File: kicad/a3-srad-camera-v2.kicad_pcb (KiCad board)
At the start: 4 copper layers, 50 x 50 mm, 179 parts, among them J1 Amphenol F32Q 1x22 P=0.5mm, J2 BOARD_IND, J3 OUT, SW1 PWRON, U1 AMS1117-3.3, U2 TPS6521905RHBR, U3 STM32U073R8Tx, U4 RV1106G2

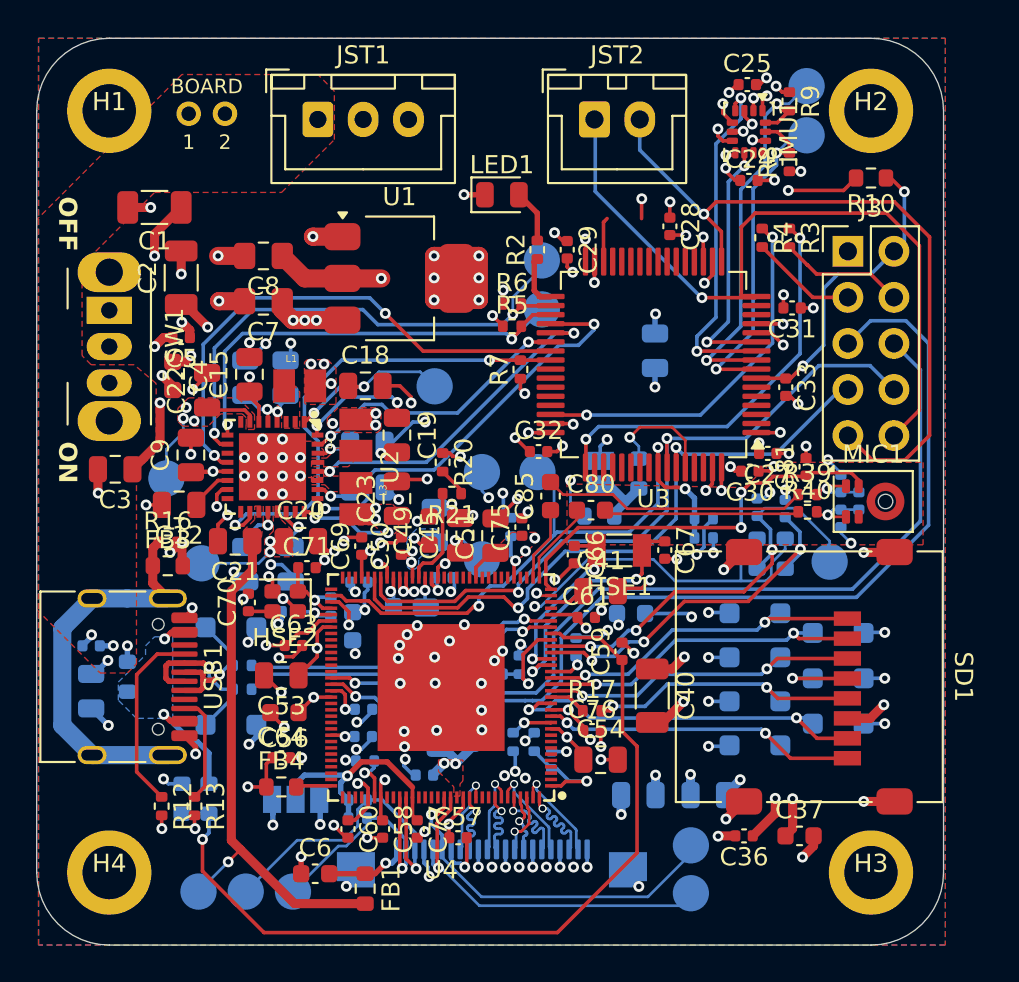
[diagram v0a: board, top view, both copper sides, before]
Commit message: Footprint + silkscreen corrections
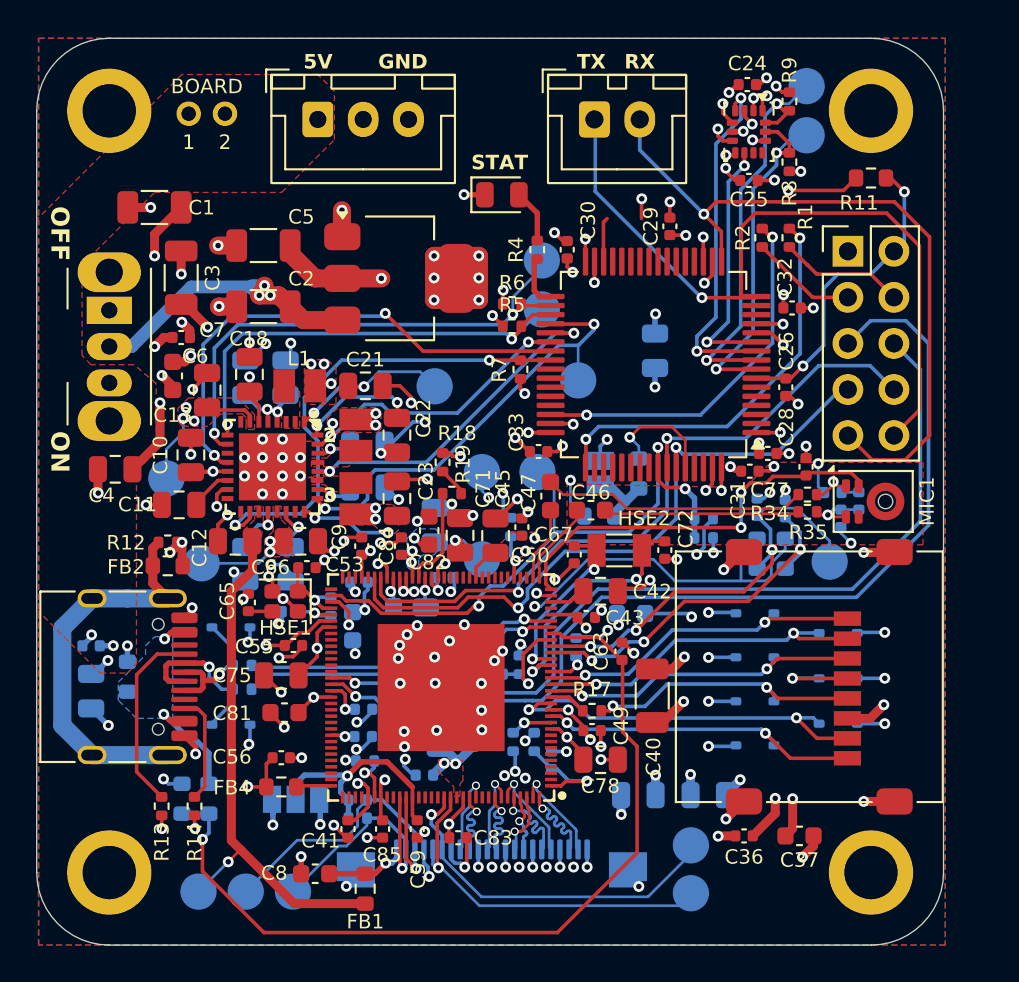
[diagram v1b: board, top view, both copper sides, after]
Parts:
- added TP9: TestPoint, a3-srad-camera-v2:TestPoint_Pad_D2.0mm_Small_Courtyard, B.Cu at (156.9, 94.9)
- C2: renamed from C7; footprint Capacitor_SMD:C_0805_2012Metric_Pad1.18x1.45mm_HandSolder -> Capacitor_SMD:C_1206_3216Metric
- C5: renamed from C8; footprint Capacitor_SMD:C_0805_2012Metric_Pad1.18x1.45mm_HandSolder -> Capacitor_SMD:C_1206_3216Metric
- D1, D2, D3, D4, D5, D6, D7, D8, D9: footprint Diode_SMD:D_SOD-123F -> Diode_SMD:D_SOD-323
- R4: renamed from R2; value ? -> 120R
- moved C68 0.67 mm to (170.9, 101.0), turned to 0 degrees
- moved C5 0.57 mm to (139.5, 87.4)
- moved C2 0.30 mm to (139.5, 90.8)
- renumbered C9 to C10, C12 to C11, C21 to C12, C22 to C13, C10 to C14, C11 to C15, C13 to C16, C14 to C17, C15 to C18, C16 to C19, C17 to C20, C18 to C21, C19 to C22, C25 to C24, C24 to C25, C33 to C26, C26 to C27, C27 to C28, C28 to C29, C2 to C3, C29 to C30, C30 to C31, C31 to C32, C32 to C33, C3 to C4, C60 to C41, C41 to C42, C61 to C43, C62 to C44, C51 to C45, C80 to C46, C85 to C47, C72 to C48, C76 to C49, C75 to C50, C73 to C51, C68 to C52, C69 to C53, C74 to C54, C63 to C55, C64 to C56, C65 to C57, C79 to C58, C77 to C59, C4 to C6, C78 to C60, C42 to C61, C43 to C62, C59 to C63, C44 to C64, C70 to C65, C71 to C66, C66 to C67, C83 to C68, C82 to C69, C5 to C7, C84 to C70, C45 to C71, C67 to C72, C52 to C73, C46 to C74, C53 to C75, C47 to C76, C81 to C77, C54 to C78, C55 to C79, C6 to C8, C48 to C80, C56 to C81, C49 to C82, C57 to C83, C50 to C84, C58 to C85, C20 to C9, FB3 to FB2, FB2 to FB3, H3 to H2, H2 to H3, HSE2 to HSE1, HSE1 to HSE2, J3 to J1, J1 to J2, J2 to J3, R3 to R1, R11 to R10, R10 to R11, R16 to R12, R12 to R13, R13 to R14, R14 to R15, R15 to R16, R20 to R18, R21 to R19, R4 to R2, R24 to R20, R18 to R21, R23 to R22, R27 to R23, R34 to R24, R30 to R25, R31 to R26, R32 to R27, R33 to R28, R37 to R29, R1 to R3, R35 to R30, R36 to R31, R19 to R32, R22 to R33, R39 to R34, R40 to R35, R28 to R36, R25 to R37, R29 to R38, R26 to R39, TP2 to TP10, TP4 to TP11, TP7 to TP12, TP9 to TP13, TP11 to TP14, TP12 to TP15, TP14 to TP16, TP16 to TP17, TP3 to TP2, TP5 to TP3, TP6 to TP4, TP8 to TP5, TP10 to TP6, TP13 to TP7, TP15 to TP8
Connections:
- C1 pad 1: VSYS_5V0 -> VIN_5V
- C10 pad 1: VSYS_5V0 -> VIN_5V
- C14 pad 1: VSYS_5V0 -> VIN_5V
- C15 pad 1: VSYS_5V0 -> VIN_5V
- C16 pad 1: VSYS_5V0 -> VIN_5V
- C17 pad 1: VSYS_5V0 -> VIN_5V
- C18 pad 1: VSYS_5V0 -> VIN_5V
- C19 pad 1: VSYS_5V0 -> VIN_5V
- C20 pad 1: VSYS_5V0 -> VIN_5V
- C3 pad 1: VSYS_5V0 -> VIN_5V
- C34 pad 2: /VIN_5V -> VIN_5V
- C35 pad 2: /VIN_5V -> VIN_5V
- C4 pad 1: VSYS_5V0 -> VIN_5V
- C6 pad 1: VSYS_5V0 -> VIN_5V
- C7 pad 2: VSYS_5V0 -> VIN_5V
- FB3 pad 1: /VIN_5V -> VIN_5V
- JST1 pad 1: /VIN_5V -> VIN_5V
- SW1 pad 3: /VIN_5V -> VIN_5V
- U2 pad 13: VSYS_5V0 -> VIN_5V
- U2 pad 20: VSYS_5V0 -> VIN_5V
- U2 pad 22: VSYS_5V0 -> VIN_5V
- U2 pad 26: VSYS_5V0 -> VIN_5V
- U2 pad 30: VSYS_5V0 -> VIN_5V
- U2 pad 4: VSYS_5V0 -> VIN_5V
- U2 pad 5: VSYS_5V0 -> VIN_5V
- U2 pad 6: VSYS_5V0 -> VIN_5V
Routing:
- net VIN_5V: track 0.00 -> 34.2 mm, vias 0 -> 16
- net VSYS_5V0: track 35.4 -> 17.7 mm, vias 16 -> 3
- net /VIN_5V: track 2.86 -> 0.00 mm, vias 3 -> 0
- net GND: track 154.3 -> 156.5 mm
- net /EN: track 23.1 -> 25.0 mm
- net /VSEL: track 28.7 -> 28.0 mm
- net /SCL: track 29.8 -> 29.1 mm
- added copper zone on F.Cu, net VIN_5V
- added copper zone on In1.Cu, net VIN_5V
- removed copper zone on F.Cu, net /VIN_5V
- removed copper zone on In1.Cu, net VSYS_5V0
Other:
- board text added: "2"
- board text added: "3"
- board text added: "5V"
- board text added: "CLK"
- board text added: "DIO"
- board text added: "FC"
- board text added: "GND"
- board text added: "RST"
- board text added: "RV"
- board text added: "RX"
- board text added: "STAT"
- board text added: "STM"
- board text added: "TX"

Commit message: Final changes before order
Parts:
- removed C68, C69, C70: 100pF, Capacitor_SMD:C_0402_1005Metric
- removed C77: 100nF, Capacitor_SMD:C_0402_1005Metric
- removed R34, R35: 22k, Resistor_SMD:R_0402_1005Metric
- added C86: 100nF, Capacitor_SMD:C_0402_1005Metric, B.Cu at (170.3, 101.1)
- added C87: 15pF, Capacitor_SMD:C_0402_1005Metric, B.Cu at (170.3, 102.0)
- added FB5: 120R, Resistor_SMD:R_0603_1608Metric, F.Cu at (169.8, 100.4)
- added R40: DNP, Resistor_SMD:R_0402_1005Metric, B.Cu at (159.4, 89.0)
- added R41: DNP, Resistor_SMD:R_0402_1005Metric, B.Cu at (159.4, 90.3)
- added R42: 10k, Resistor_SMD:R_0402_1005Metric, F.Cu at (151.4, 95.9)
- added R43: DNP, Resistor_SMD:R_0402_1005Metric, F.Cu at (151.4, 94.9)
- C46, C47: value 1uF -> 100nF; footprint Capacitor_SMD:C_0603_1608Metric -> Capacitor_SMD:C_0402_1005Metric
- MIC1: value IM73A135V01 -> CMM-2718AB-3815NC-TR; footprint Sensor_Audio:Infineon_PG-LLGA-5-2 -> a3-srad-camera-v2:MIC_CMM-2718AB-3815NC-TR
- moved C47 0.38 mm to (155.3, 101.6)
- moved C46 0.18 mm to (157.6, 102.2)
- moved MIC1 0.12 mm to (173.0, 101.5), turned to 90 degrees
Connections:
- net /STM32U575RGT6/BOOT0 renamed /STM32U073x/BOOT0
- net /STM32U575RGT6/LED renamed /STM32U073x/LED
- net /STM32U575RGT6/SWCLK renamed /STM32U073x/SWCLK
- net /STM32U575RGT6/SWDIO renamed /STM32U073x/SWDIO
- net /TPS6521905RHBR/LX_B1_1 renamed /TPS65219x/LX_B1
- net /TPS6521905RHBR/LX_B2 renamed /TPS65219x/LX_B2
- net /TPS6521905RHBR/LX_B3 renamed /TPS65219x/LX_B3
- MIC1 pad 2: /RV1106G2 SoC/VCC1V8_MICBIAS -> /RV1106G2 SoC/CODEC_MIC0P
- MIC1 pad 3: Net-(MIC1-OUT-) -> GND
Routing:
- net /RV1106G2 SoC/CODEC_MIC0N: track 10.8 -> 15.4 mm
- net /RV1106G2 SoC/VCC1V8_MICBIAS: track 22.6 -> 18.6 mm
- net Net-(MIC1-OUT-): track 3.56 -> 0.00 mm, vias 1 -> 0
- net VSYS_3V3: track 43.7 -> 47.2 mm, vias 32 -> 34
- net /EN: track 25.0 -> 28.3 mm
- net /VDD_CPU: track 12.1 -> 8.80 mm
- net /RV1106G2 SoC/CODEC_MIC0P: track 14.6 -> 17.7 mm, vias 0 -> 1
- net /VSEL: track 28.0 -> 30.6 mm
- net GND: track 156.5 -> 155.6 mm
- net Net-(MIC1-VDD): track 3.76 -> 2.91 mm
- net VCC_3V3_RK: vias 20 -> 19
- added copper zone on B.Cu, net /VDD_CPU
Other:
- board text added: "1"
- board text added: "22"
- board text added: "DNP"
- board text added: "OPT"
